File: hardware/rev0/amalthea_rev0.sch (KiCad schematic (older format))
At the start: 26 parts, among them J1 USB_B_Micro, J2 USB_B_Micro, J3 Conn_Coaxial, J4 Conn_Coaxial, J7 Conn_02x02_Counter_Clockwise, J8 Conn_Coaxial, J9 Conn_Coaxial, SW1 BTN_RECOVERY, SW2 BTN_DFU, SW3 BTN_RESET, Y1 DSC60xx

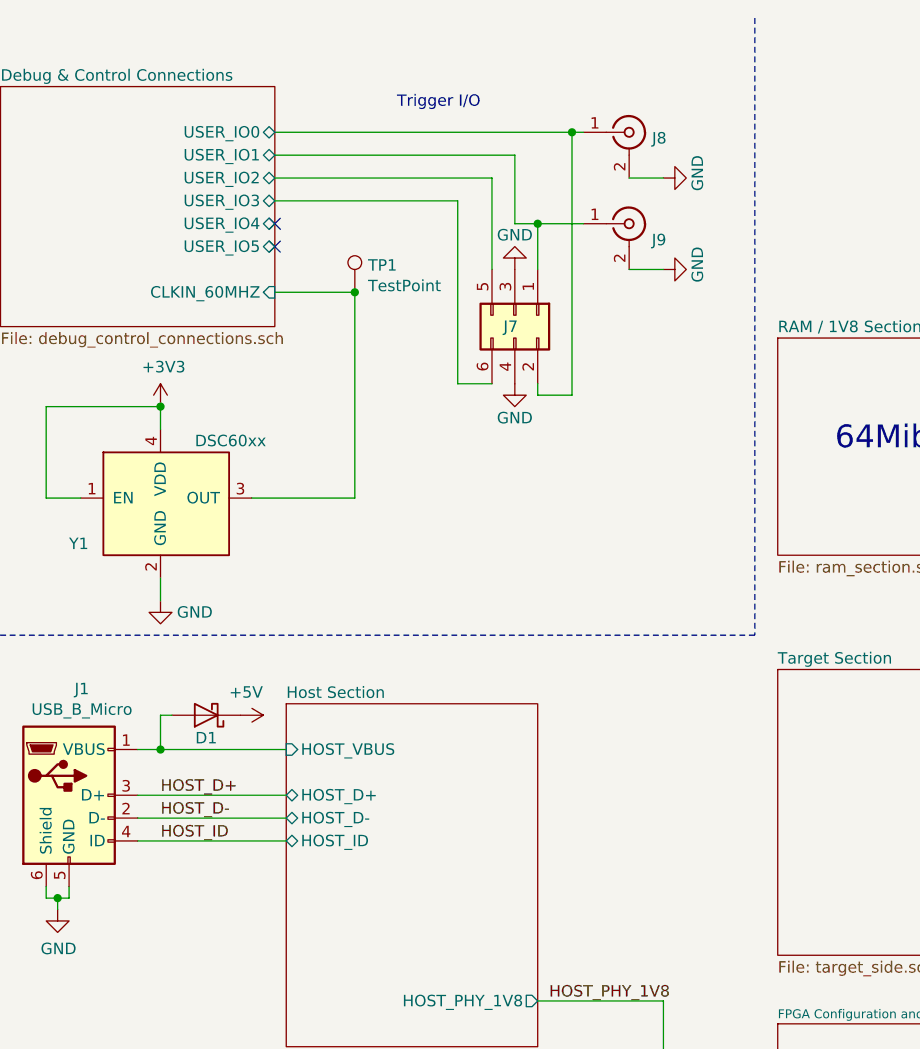
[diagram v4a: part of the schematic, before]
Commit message: Start re-arranging user IO
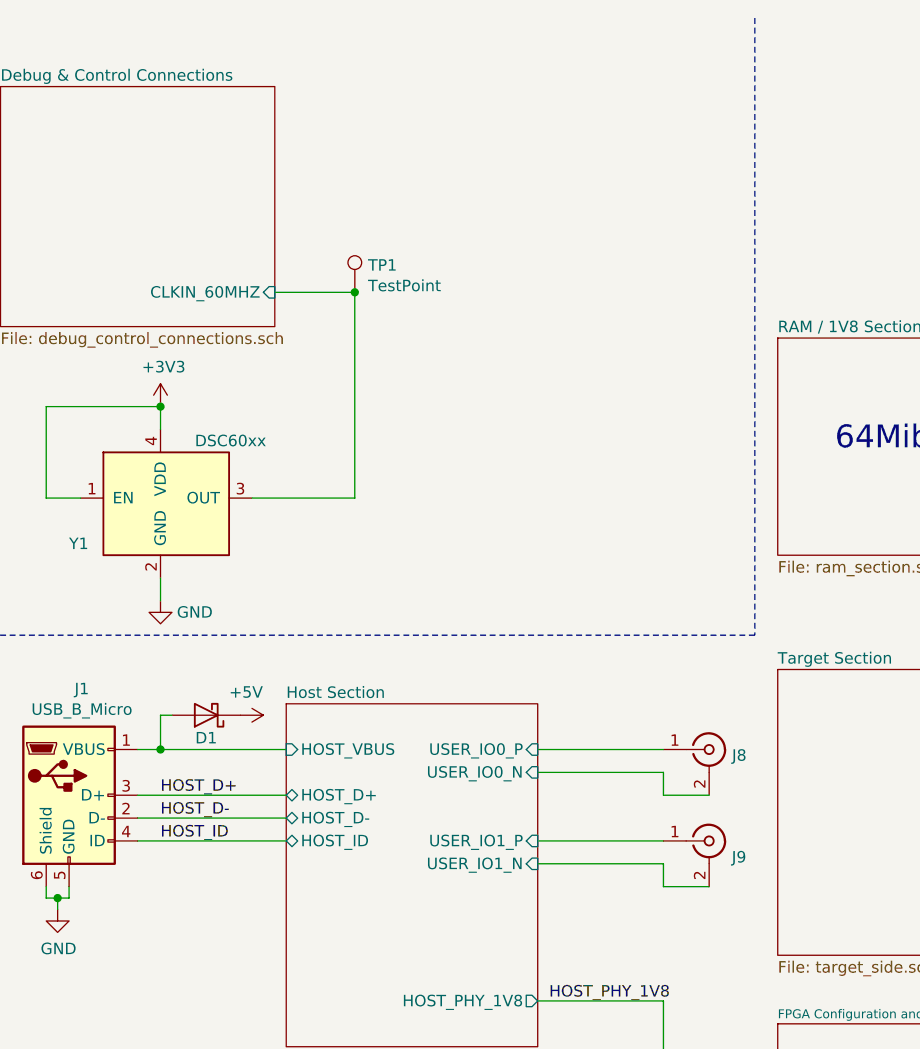
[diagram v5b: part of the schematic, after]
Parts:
- removed J7: Conn_02x02_Counter_Clockwise, Connector_PinHeader_2.54mm:PinHeader_2x03_P2.54mm_Horizontal, symbol Connector_Generic:Conn_02x03_Odd_Even
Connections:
- net GND: no longer J8.2 (Ext), J9.2 (Ext)
- net Debug & Control Connections/USER_IO0 renamed Host Section/USER_IO0_P
- net Debug & Control Connections/USER_IO1 renamed Host Section/USER_IO1_P
- new net Host Section/USER_IO0_N: J8.2 (Ext)
- new net Host Section/USER_IO1_N: J9.2 (Ext)
- no-connect marks 2 -> 0
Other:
- note removed: "Trigger I/O"
- moved on the sheet: J8, J9
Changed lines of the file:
@@
 F5 "HOST_VBUS" I L 1850 3700 50
 F6 "HOST_PHY_1V8" O R 2950 4800 50
+F7 "USER_IO0_P" I R 2950 3700 50
+F8 "USER_IO0_N" I R 2950 3800 50
+F9 "USER_IO1_N" I R 2950 4200 50
+F10 "USER_IO1_P" I R 2950 4100 50
 $EndSheet
 Wire Wire Line
@@
 	10500 5100 10700 5100
 $Comp
-L power:GND #PWR0111
-U 1 1 5E2A5843
-P 2850 2100
-F 0 "#PWR0111" H 2850 1850 50  0001 C CNN
-F 1 "GND" H 2850 1950 50  0000 C CNN
-F 2 "" H 2850 2100 50  0001 C CNN
-F 3 "" H 2850 2100 50  0001 C CNN
-	1    2850 2100
-	1    0    0    -1
-$EndComp
-$Comp
-L power:GND #PWR0110
-U 1 1 5E2A54E0
-P 2850 1600
-F 0 "#PWR0110" H 2850 1350 50  0001 C CNN
-F 1 "GND" H 2850 1450 50  0000 C CNN
-F 2 "" H 2850 1600 50  0001 C CNN
-F 3 "" H 2850 1600 50  0001 C CNN
-	1    2850 1600
-	-1   0    0    1
-$EndComp
-Wire Wire Line
-	3100 1000 3150 1000
-Connection ~ 3100 1000
-Wire Wire Line
-	3100 2150 3100 1000
-Wire Wire Line
-	2950 2150 3100 2150
-Wire Wire Line
-	2950 2100 2950 2150
-Wire Wire Line
-	2950 1400 3150 1400
-Wire Wire Line
-	1800 1000 3100 1000
-$Comp
 L Connector:Conn_Coaxial J8
 U 1 1 5E41D377
-P 3350 1000
-F 0 "J8" H 3450 974 50  0000 L CNN
-F 1 "Conn_Coaxial" H 3450 884 50  0001 L CNN
-F 2 "amalthea:SMA-EDGE" H 3350 1000 50  0001 C CNN
-F 3 " ~" H 3350 1000 50  0001 C CNN
-	1    3350 1000
-	1    0    0    -1
-$EndComp
-Wire Wire Line
-	3500 1200 3350 1200
-Connection ~ 2950 1400
-Wire Wire Line
-	2950 1400 2950 1600
-Wire Wire Line
-	2850 1400 2950 1400
-Wire Wire Line
-	2850 1100 1800 1100
-Wire Wire Line
-	2850 1400 2850 1100
-Wire Wire Line
-	1800 1200 2750 1200
-Wire Wire Line
-	2750 1200 2750 1600
-Wire Wire Line
-	1800 1300 2600 1300
-Wire Wire Line
-	2600 2100 2750 2100
-Wire Wire Line
-	2600 1300 2600 2100
-Text Notes 2700 900  2    50   ~ 0
-Trigger I/O
-$Comp
-L Connector_Generic:Conn_02x03_Odd_Even J7
-U 1 1 5E44B790
-P 2850 1800
-F 0 "J7" V 2900 1750 50  0000 L CNN
-F 1 "Conn_02x02_Counter_Clockwise" V 2945 1879 50  0001 L CNN
-F 2 "Connector_PinHeader_2.54mm:PinHeader_2x03_P2.54mm_Horizontal" H 2850 1800 50  0001 C CNN
-F 3 "~" H 2850 1800 50  0001 C CNN
-	1    2850 1800
-	0    1    1    0
-$EndComp
-Wire Wire Line
-	3500 1600 3350 1600
-$Comp
-L power:GND #PWR0107
-U 1 1 5E440A75
-P 3500 1600
-F 0 "#PWR0107" H 3500 1350 50  0001 C CNN
-F 1 "GND" H 3600 1450 50  0000 R CNN
-F 2 "" H 3500 1600 50  0001 C CNN
-F 3 "" H 3500 1600 50  0001 C CNN
-	1    3500 1600
-	0    -1   -1   0
-$EndComp
-$Comp
-L power:GND #PWR0106
-U 1 1 5E43820F
-P 3500 1200
-F 0 "#PWR0106" H 3500 950 50  0001 C CNN
-F 1 "GND" H 3600 1050 50  0000 R CNN
-F 2 "" H 3500 1200 50  0001 C CNN
-F 3 "" H 3500 1200 50  0001 C CNN
-	1    3500 1200
-	0    -1   -1   0
+P 3700 3700
+F 0 "J8" H 3800 3674 50  0000 L CNN
+F 1 "Conn_Coaxial" H 3800 3584 50  0001 L CNN
+F 2 "amalthea:SMA-EDGE" H 3700 3700 50  0001 C CNN
+F 3 " ~" H 3700 3700 50  0001 C CNN
+	1    3700 3700
+	1    0    0    -1
 $EndComp
 $Comp
 L Connector:Conn_Coaxial J9
 U 1 1 5E41DB94
-P 3350 1400
-F 0 "J9" H 3449 1329 50  0000 L CNN
-F 1 "Conn_Coaxial" H 3450 1284 50  0001 L CNN
-F 2 "amalthea:SMA-EDGE" H 3350 1400 50  0001 C CNN
-F 3 " ~" H 3350 1400 50  0001 C CNN
-	1    3350 1400
+P 3700 4100
+F 0 "J9" H 3799 4029 50  0000 L CNN
+F 1 "Conn_Coaxial" H 3800 3984 50  0001 L CNN
+F 2 "amalthea:SMA-EDGE" H 3700 4100 50  0001 C CNN
+F 3 " ~" H 3700 4100 50  0001 C CNN
+	1    3700 4100
 	1    0    0    -1
 $EndComp
@@
 Wire Wire Line
 	2150 1700 2150 2600
-NoConn ~ 1800 1400
 $Sheet
 S 600  800  1200 1050
@@
 F1 "debug_control_connections.sch" 50
 F2 "CLKIN_60MHZ" I R 1800 1700 50
-F3 "USER_IO0" B R 1800 1000 50
-F4 "USER_IO1" B R 1800 1100 50
-F5 "USER_IO2" B R 1800 1200 50
-F6 "USER_IO3" B R 1800 1300 50
-F7 "USER_IO4" B R 1800 1400 50
-F8 "USER_IO5" B R 1800 1500 50
 $EndSheet
-NoConn ~ 1800 1500
 $Sheet
 S 8200 4800 800  1450
@@
 	1    0    0    -1
 $EndComp
+Wire Wire Line
+	2950 3700 3500 3700
+Wire Wire Line
+	2950 3800 3500 3800
+Wire Wire Line
+	3500 3800 3500 3900
+Wire Wire Line
+	3500 3900 3700 3900
+Wire Wire Line
+	2950 4100 3500 4100
+Wire Wire Line
+	2950 4200 3500 4200
+Wire Wire Line
+	3500 4200 3500 4300
+Wire Wire Line
+	3500 4300 3700 4300
 $EndSCHEMATC

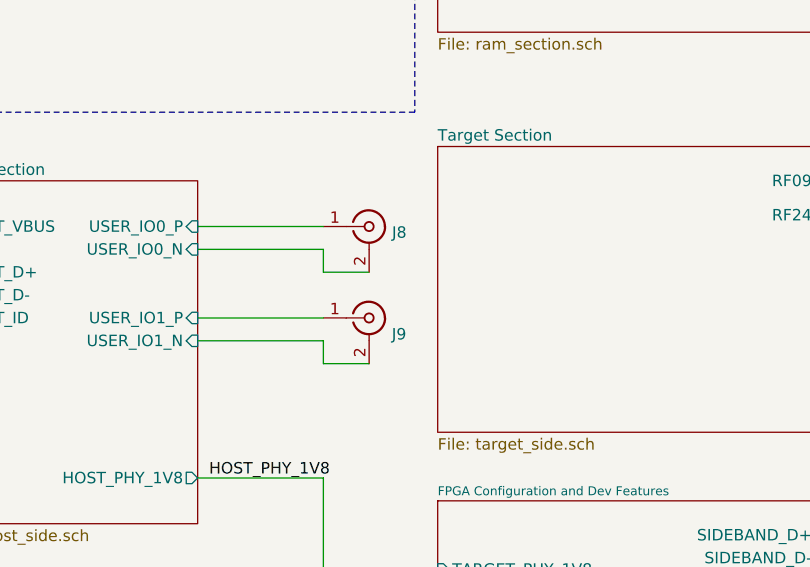
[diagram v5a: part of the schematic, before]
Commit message: Route LVDS user IO
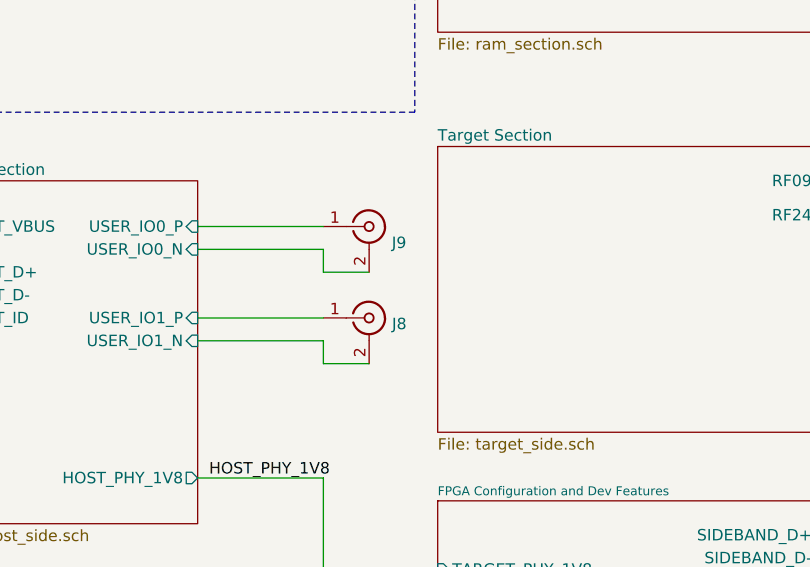
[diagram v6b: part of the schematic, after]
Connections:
- net Host Section/USER_IO0_N: now also J9.2 (Ext); no longer J8.2 (Ext)
- net Host Section/USER_IO0_P: now also J9.1 (In); no longer J8.1 (In)
- net Host Section/USER_IO1_N: now also J8.2 (Ext); no longer J9.2 (Ext)
- net Host Section/USER_IO1_P: now also J8.1 (In); no longer J9.1 (In)
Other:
- moved on the sheet: J8, J9
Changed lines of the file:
@@
 L Connector:Conn_Coaxial J8
 U 1 1 5E41D377
+P 3700 4100
+F 0 "J8" H 3800 4074 50  0000 L CNN
+F 1 "Conn_Coaxial" H 3800 3984 50  0001 L CNN
+F 2 "amalthea:SMA-EDGE" H 3700 4100 50  0001 C CNN
+F 3 " ~" H 3700 4100 50  0001 C CNN
+	1    3700 4100
+	1    0    0    -1
+$EndComp
+$Comp
+L Connector:Conn_Coaxial J9
+U 1 1 5E41DB94
 P 3700 3700
-F 0 "J8" H 3800 3674 50  0000 L CNN
+F 0 "J9" H 3799 3629 50  0000 L CNN
 F 1 "Conn_Coaxial" H 3800 3584 50  0001 L CNN
 F 2 "amalthea:SMA-EDGE" H 3700 3700 50  0001 C CNN
@@
 	1    0    0    -1
 $EndComp
-$Comp
-L Connector:Conn_Coaxial J9
-U 1 1 5E41DB94
-P 3700 4100
-F 0 "J9" H 3799 4029 50  0000 L CNN
-F 1 "Conn_Coaxial" H 3800 3984 50  0001 L CNN
-F 2 "amalthea:SMA-EDGE" H 3700 4100 50  0001 C CNN
-F 3 " ~" H 3700 4100 50  0001 C CNN
-	1    3700 4100
-	1    0    0    -1
-$EndComp

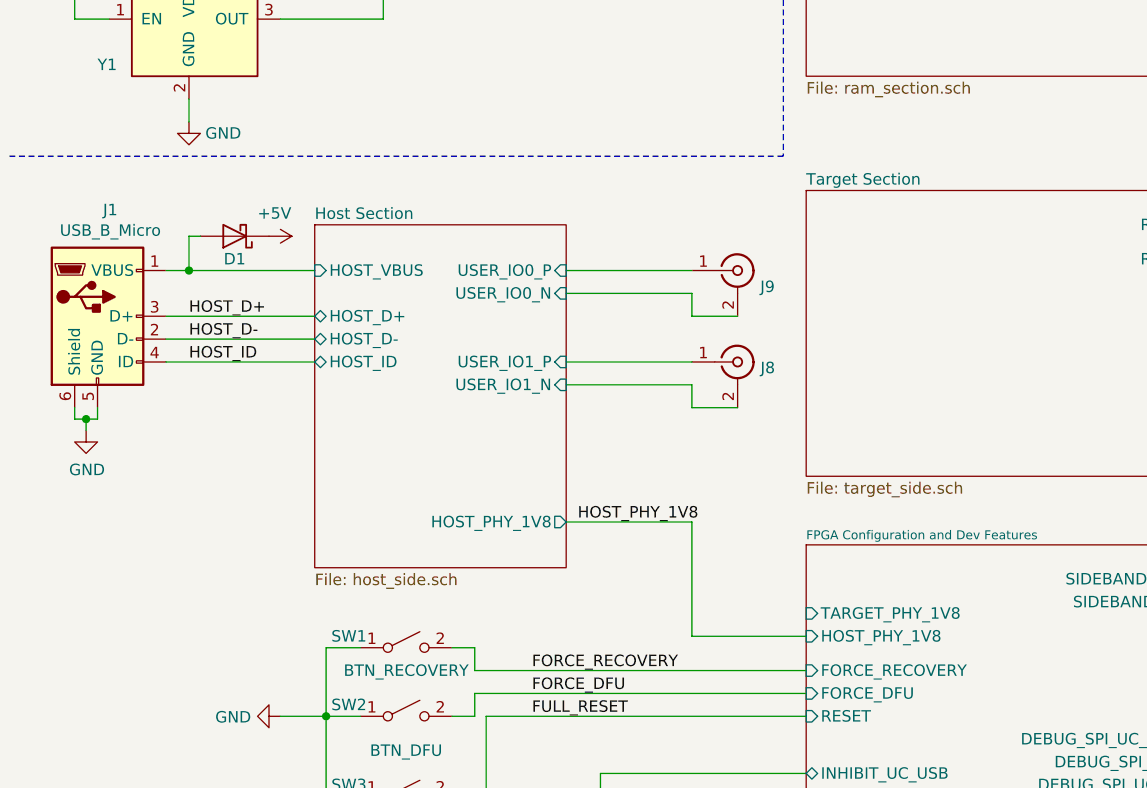
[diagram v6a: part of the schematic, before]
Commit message: Route/NC remaining target signals, ERC & schematic cleanup
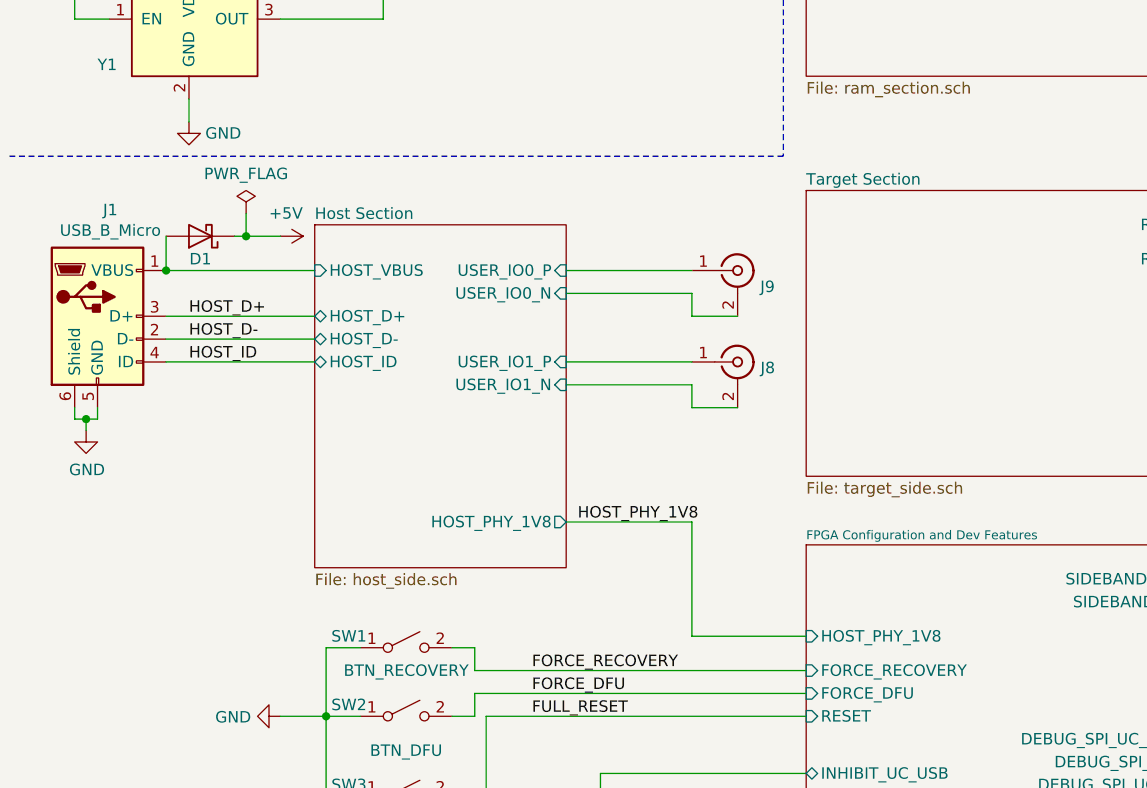
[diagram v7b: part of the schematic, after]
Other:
- moved on the sheet: D1
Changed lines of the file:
@@
 F7 "SIDEBAND_PHY_1V8" I L 4000 6000 50
 F8 "HOST_PHY_1V8" I L 4000 5300 50
-F9 "TARGET_PHY_1V8" I L 4000 5200 50
-F10 "FORCE_RECOVERY" I L 4000 5450 50
-F11 "FORCE_DFU" I L 4000 5550 50
-F12 "INHIBIT_UC_USB" B L 4000 5900 50
-F13 "RESET" I L 4000 5650 50
-F14 "UC_TX_FPGA_RX" O R 5700 6200 50
-F15 "UC_RX_FPGA_TX" I R 5700 6300 50
-F16 "DEBUG_SPI_CS" O R 5700 6050 50
+F9 "FORCE_RECOVERY" I L 4000 5450 50
+F10 "FORCE_DFU" I L 4000 5550 50
+F11 "INHIBIT_UC_USB" B L 4000 5900 50
+F12 "RESET" I L 4000 5650 50
+F13 "UC_TX_FPGA_RX" O R 5700 6200 50
+F14 "UC_RX_FPGA_TX" I R 5700 6300 50
+F15 "DEBUG_SPI_CS" O R 5700 6050 50
 $EndSheet
 Text Label 5950 5050 0    50   ~ 0
@@
 	850  4350 900  4350
 Wire Wire Line
-	1850 3700 1300 3700
+	1850 3700 1200 3700
 Wire Wire Line
 	1200 3900 1850 3900
@@
 L Device:D_Schottky D1
 U 1 1 5DDCCE15
-P 1500 3550
-F 0 "D1" H 1500 3650 50  0000 C CNN
-F 1 "PMEG3050EP,115" H 1400 3700 50  0001 C CNN
-F 2 "amalthea:SOD128" H 1500 3550 50  0001 C CNN
-F 3 "~" H 1500 3550 50  0001 C CNN
-	1    1500 3550
+P 1350 3550
+F 0 "D1" H 1350 3650 50  0000 C CNN
+F 1 "PMEG3050EP,115" H 1250 3700 50  0001 C CNN
+F 2 "amalthea:SOD128" H 1350 3550 50  0001 C CNN
+F 3 "~" H 1350 3550 50  0001 C CNN
+	1    1350 3550
 	-1   0    0    1
 $EndComp
 Wire Wire Line
-	1350 3550 1300 3550
-Wire Wire Line
-	1300 3550 1300 3700
-Connection ~ 1300 3700
-Wire Wire Line
-	1300 3700 1200 3700
+	1200 3550 1200 3700
+Connection ~ 1200 3700
 $Sheet
 S 4000 3350 1700 1250
@@
 L power:+5V #PWR0113
 U 1 1 5E2D79BC
-P 1650 3550
-F 0 "#PWR0113" H 1650 3400 50  0001 C CNN
-F 1 "+5V" V 1550 3500 50  0000 L CNN
-F 2 "" H 1650 3550 50  0001 C CNN
-F 3 "" H 1650 3550 50  0001 C CNN
-	1    1650 3550
+P 1700 3550
+F 0 "#PWR0113" H 1700 3400 50  0001 C CNN
+F 1 "+5V" V 1600 3500 50  0000 L CNN
+F 2 "" H 1700 3550 50  0001 C CNN
+F 3 "" H 1700 3550 50  0001 C CNN
+	1    1700 3550
 	0    1    1    0
 $EndComp
@@
 Wire Wire Line
 	3500 4300 3700 4300
+$Comp
+L power:PWR_FLAG #FLG0101
+U 1 1 5EE01800
+P 1550 3450
+F 0 "#FLG0101" H 1550 3525 50  0001 C CNN
+F 1 "PWR_FLAG" H 1550 3623 50  0000 C CNN
+F 2 "" H 1550 3450 50  0001 C CNN
+F 3 "~" H 1550 3450 50  0001 C CNN
+	1    1550 3450
+	1    0    0    -1
+$EndComp
+Wire Wire Line
+	1500 3550 1550 3550
+Wire Wire Line
+	1550 3450 1550 3550
+Connection ~ 1550 3550
+Wire Wire Line
+	1550 3550 1700 3550
 $EndSCHEMATC
